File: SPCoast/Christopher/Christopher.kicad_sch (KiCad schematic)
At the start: 45 parts, among them SW813 813, SW815 815, SW817 817, SW900 815A

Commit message: chore(kicad): masts and maintainer calls carry no CP; IRJ-Signals do; CMRInet Kind is CMRI
Owner decision: an IRJ-Signal is the single source of a signal's control point
(a mast attaches to exactly one IRJ-Signal through its SIGNAL pin); a
maintainer call is tied to its house by the netlist.
- CP dropped from 23 masts and 5 maintainer calls.
- 7 empty IRJ-Signal CPs filled with the plant's only house (Corporal, Sargent).
- 43 empty Name fields that KiCad re-added to Christopher dropped again.
- Codeline-Transport Kind CMRInet -> CMRI on the placed instance and the
  embedded library copy (South-cTc root sheet).

Verified: per-symbol before/after comparison shows only these changes; every
IRJ-Signal in all seven plants has a CP naming one of its plant's houses; net
counts unchanged (Christopher 33, Corporal 26, GilroyCalTrain 27,
GilroyInterchange 22, Luchessa 34, Sargent 18, Watsonville 96, South-cTc 341);
desk compiles to 75 appliances, 137 bindings, 14 columns. Remaining CP
diagnostic: Sargent's Corporal:2NAT placeholder (cross-plant reference).

Co-Authored-By: Claude Sonnet 5.5 <noreply@anthropic.com>
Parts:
- MC1, S3, S4, S5, S6: CP Christopher North -> (none)
- MC2: CP Christopher South -> (none)

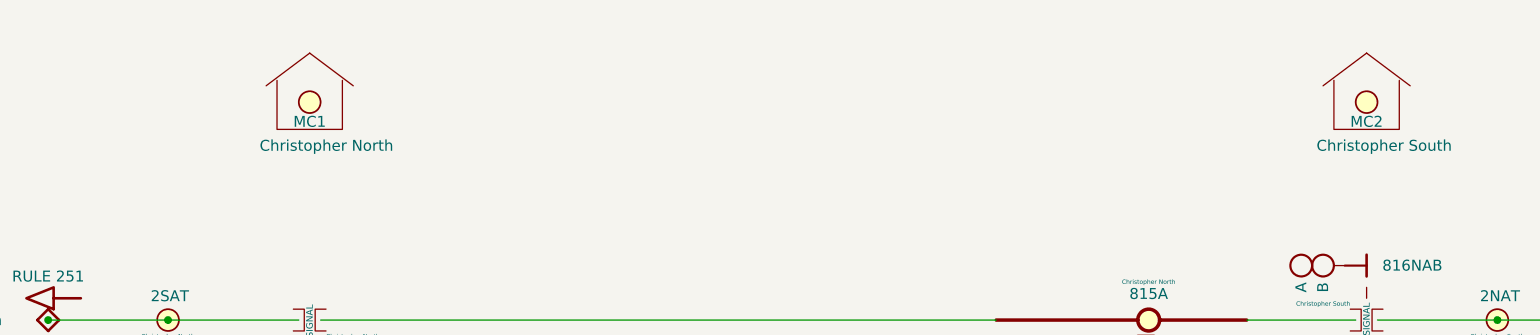
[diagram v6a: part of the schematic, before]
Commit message: SPCoast: owner's edits: Interlocking symbol on every Trackplan; MAIN HOUSE is STRUCTURE/CONTROL_POINT (baseline)
Each plant has one Interlocking symbol (Value is the authoritative name) and
every MAIN HOUSE's Interlocking pin is wired to it. Library Role/Kind:
Interlocking is STRUCTURE/INTERLOCKING, MAIN HOUSE is STRUCTURE/CONTROL_POINT
(refreshed on all instances by the owner).

Verified: one Interlocking symbol per plant; every house shares a net with it;
net counts are one higher than before in each plant (Christopher 34, Corporal
27, GilroyCalTrain 28, GilroyInterchange 23, Luchessa 35, Sargent 19,
Watsonville 97); no root-UUID regression; no symbol moved or removed.

Co-Authored-By: Claude Sonnet 5.5 <noreply@anthropic.com>
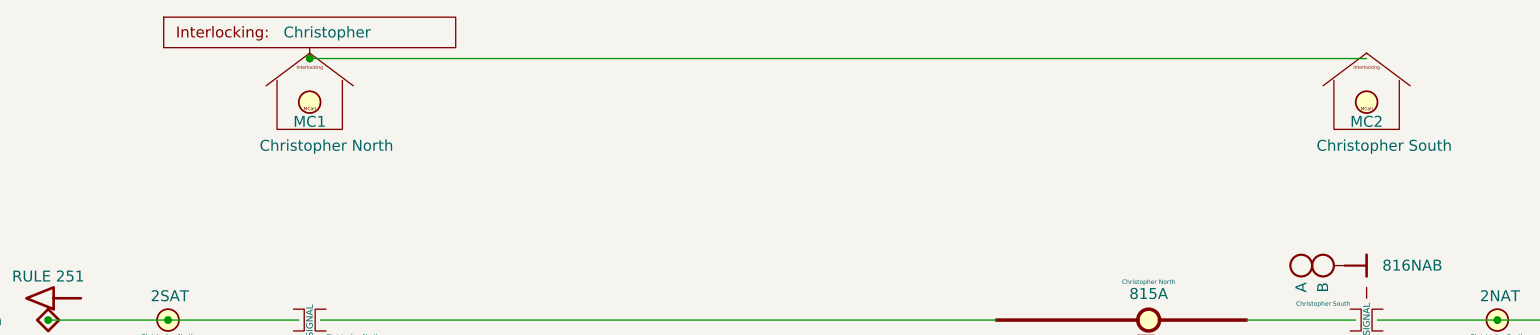
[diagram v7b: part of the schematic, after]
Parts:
- added Plant1: ${TITLE}, symbol Railroad:Interlocking
- HOUSE1, HOUSE3: Kind (none) -> CONTROL_POINT; Role CONTROL_POINT -> STRUCTURE
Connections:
- new net: HOUSE1.2 (Interlocking), HOUSE3.2 (Interlocking), Plant1.1 (Interlocking)
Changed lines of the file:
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@@
+	)
+	(junction
+		(at 72.39 36.83)
+		(diameter 0)
+		(color 0 0 0 0)
 	)
 	(junction
@@
 			(type dash)
 			(color 72 72 72 1)
+		)
+	)
+	(wire
+		(pts
+			(xy 72.39 36.83) (xy 195.58 36.83)
+		)
+		(stroke
+			(width 0)
+			(type default)
 		)
 	)
@@
 			)
 		)
-		(property "Description" "Rrepresents the Control Point Maintainer Bungalow (plus optional Maintainer Call)"
+		(property "Description" "The Control Point Maintainer Bungalow (plus optional Maintainer Call)"
 			(at 195.58 47.625 0)
 			(hide yes)
@@
 			)
 		)
-		(property "Role" "CONTROL_POINT"
-			(at 195.58 41.91 0)
+		(property "Role" "STRUCTURE"
+			(at 180.34 39.37 0)
+			(hide yes)
+			(show_name no)
+			(do_not_autoplace no)
+			(effects
+				(font
+					(size 1.27 1.27)
+				)
+			)
+		)
+		(property "Kind" "CONTROL_POINT"
+			(at 182.245 41.402 0)
 			(hide yes)
 			(show_name no)
@@
 		)
 		(pin "1"
+		)
+		(pin "2"
 		)
 		(instances
@@
 	)
 	(symbol
+		(lib_id "Railroad:Interlocking")
+		(at 72.39 36.83 0)
+		(unit 1)
+		(body_style 1)
+		(exclude_from_sim no)
+		(in_bom yes)
+		(on_board yes)
+		(in_pos_files yes)
+		(dnp no)
+		(fields_autoplaced yes)
+		(property "Reference" "Plant1"
+			(at 58.166 30.988 0)
+			(hide yes)
+			(show_name no)
+			(do_not_autoplace no)
+			(effects
+				(font
+					(size 1.27 1.27)
+				)
+			)
+		)
+		(property "Value" "${TITLE}"
+			(at 69.342 33.782 0)
+			(show_name no)
+			(do_not_autoplace yes)
+			(effects
+				(font
+					(size 1.27 1.27)
+				)
+				(justify left)
+			)
+		)
+		(property "Footprint" ""
+			(at 72.39 36.83 0)
+			(hide yes)
+			(show_name no)
+			(do_not_autoplace no)
+			(effects
+				(font
+					(size 1.27 1.27)
+				)
+			)
+		)
+		(property "Datasheet" ""
+			(at 72.39 36.83 0)
+			(hide yes)
+			(show_name no)
+			(do_not_autoplace no)
+			(effects
+				(font
+					(size 1.27 1.27)
+				)
+			)
+		)
+		(property "Description" ""
+			(at 72.39 36.83 0)
+			(hide yes)
+			(show_name no)
+			(do_not_autoplace no)
+			(effects
+				(font
+					(size 1.27 1.27)
+				)
+			)
+		)
+		(property "Role" "STRUCTURE"
+			(at 61.087 27.178 0)
+			(hide yes)
+			(show_name no)
+			(do_not_autoplace no)
+			(effects
+				(font
+					(size 1.27 1.27)
+				)
+			)
+		)
+		(property "Kind" "INTERLOCKING"
+			(at 62.484 28.829 0)
+			(hide yes)
+			(show_name no)
+			(do_not_autoplace no)
+			(effects
+				(font
+					(size 1.27 1.27)
+				)
+			)
+		)
+		(pin "1"
+		)
+		(instances
+			(project "Christopher"
+				(path "/a1d80453-f1a2-4732-9b7c-c78b77308237"
+					(reference "Plant1")
+					(unit 1)
+				)
+			)
+		)
+	)
+	(symbol
 		(lib_id "Railroad:Switch_Powered")
 		(at 132.08 100.33 0)
@@
 			)
 		)
-		(property "Description" "Rrepresents the Control Point Maintainer Bungalow (plus optional Maintainer Call)"
+		(property "Description" "The Control Point Maintainer Bungalow (plus optional Maintainer Call)"
 			(at 72.39 47.625 0)
 			(hide yes)
@@
 			)
 		)
-		(property "Role" "CONTROL_POINT"
-			(at 72.39 41.91 0)
+		(property "Role" "STRUCTURE"
+			(at 57.15 39.37 0)
+			(hide yes)
+			(show_name no)
+			(do_not_autoplace no)
+			(effects
+				(font
+					(size 1.27 1.27)
+				)
+			)
+		)
+		(property "Kind" "CONTROL_POINT"
+			(at 59.055 41.402 0)
 			(hide yes)
 			(show_name no)
@@
 		(pin "1"
 		)
+		(pin "2"
+		)
 		(instances

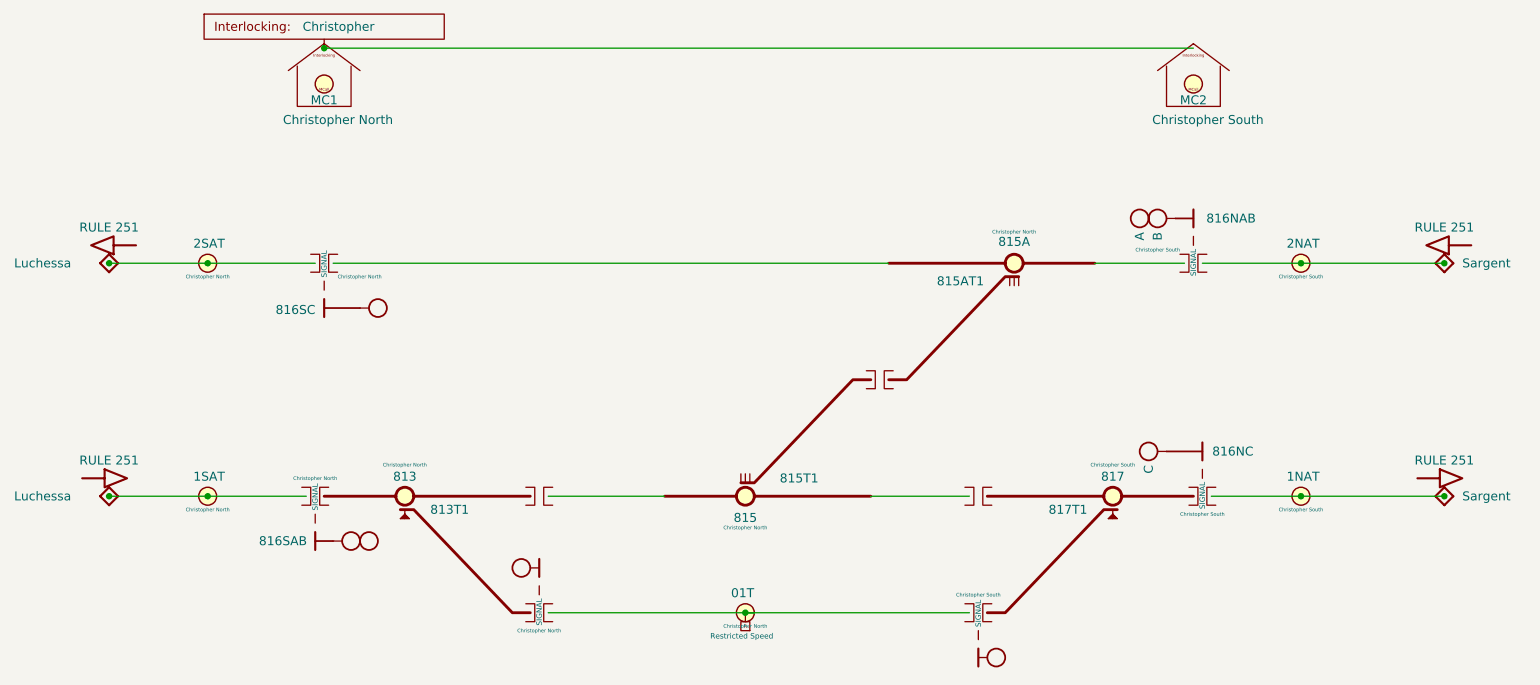
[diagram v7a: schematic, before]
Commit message: SPCoast: owner's edits: NextCP names, Christopher heads and masts, Sargent milepost, Watsonville circuits and desk tokens (baseline)
- NextCP values name interlockings: GilroyCalTrain CP2 -> Gilroy Interchange;
  Luchessa CP1 -> Gilroy Interchange, CP2 -> Hollister, CP3 and CP4 ->
  Christopher.
- Christopher: the two unnamed dwarf masts, their IRJ-Signals (now plain IRJs)
  and heads removed; remaining heads lettered A, B, C.
- Sargent MAIN HOUSE Milepost 83.5.
- Watsonville circuits SDT -> 0DT and SAT -> 0AT; desk tokens 0DT, 0AT, AT and
  Watsonville:837T1 follow.

Verified: netlists rebuild (Christopher 30, Corporal 27, GilroyCalTrain 28,
GilroyInterchange 23, Luchessa 35, Sargent 19, Watsonville 97, South-cTc 341);
Christopher has no mast or head diagnostics left; desk compiles to 75
appliances, 137 bindings, 14 columns; no root-UUID regression.

Co-Authored-By: Claude Sonnet 5.5 <noreply@anthropic.com>
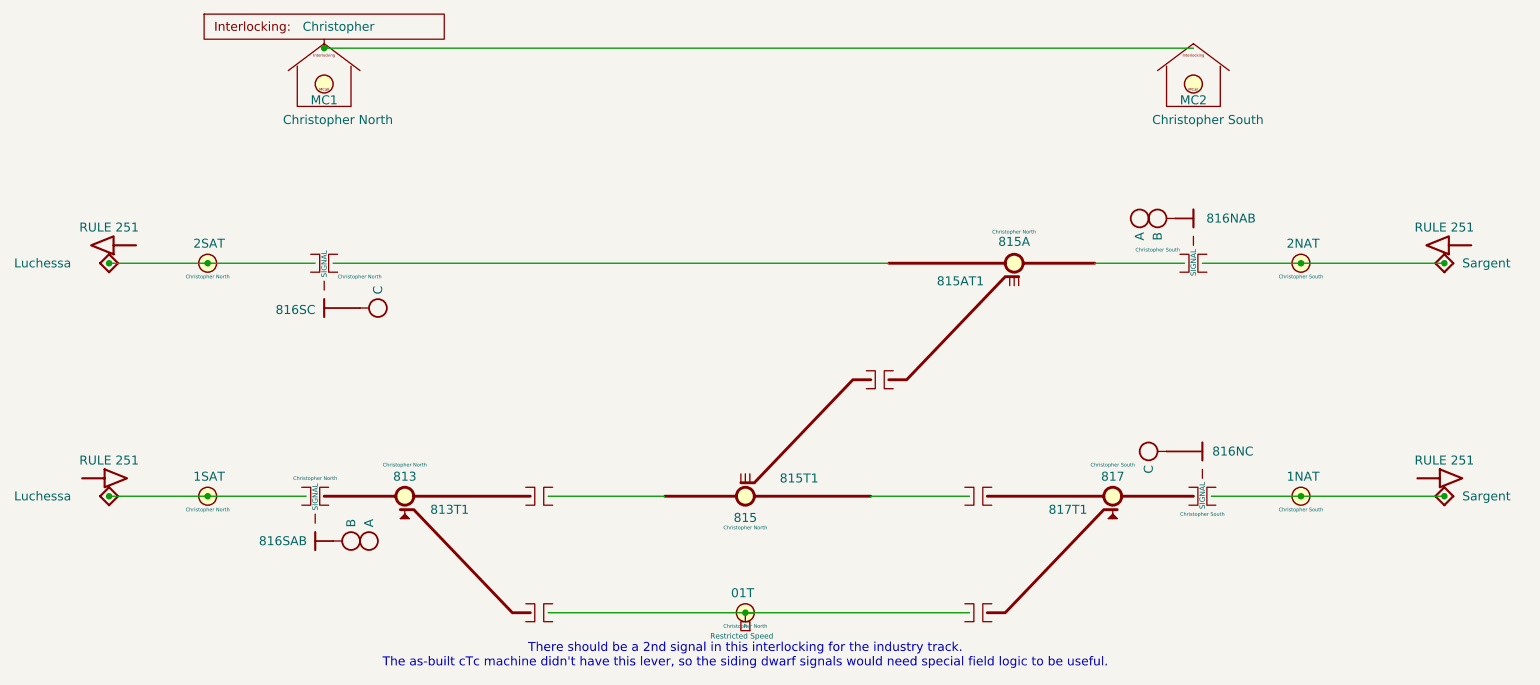
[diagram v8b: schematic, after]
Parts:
- removed B8, B9: (no value), symbol Railroad:IRJ-Signal
- removed H1, H2: (no value), symbol Railroad:Signal Head - CL
- removed S1, S2: (no value), symbol Railroad:Mast_Dwarf
- added B8, B9: (no value), symbol Railroad:IRJ
- H5: value (none) -> A
- H6: value (none) -> B
- H8: value (none) -> C
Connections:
- net at SW813.3 (R): now also B8.1 (A)
- net at DOT5.1 (To), TC5.1 (TC): now also B8.2 (B), B9.1 (A)
- net at SW817.3 (R): now also B9.2 (B)
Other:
- note added: "There should be a 2nd signal in this interlocking for the industry track. The as-built cTc machine didn't have this lever, so the siding dwarf signals would need special field logic to be useful."
